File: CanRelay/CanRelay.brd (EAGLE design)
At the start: 70.7 x 62.9 mm, 20 parts

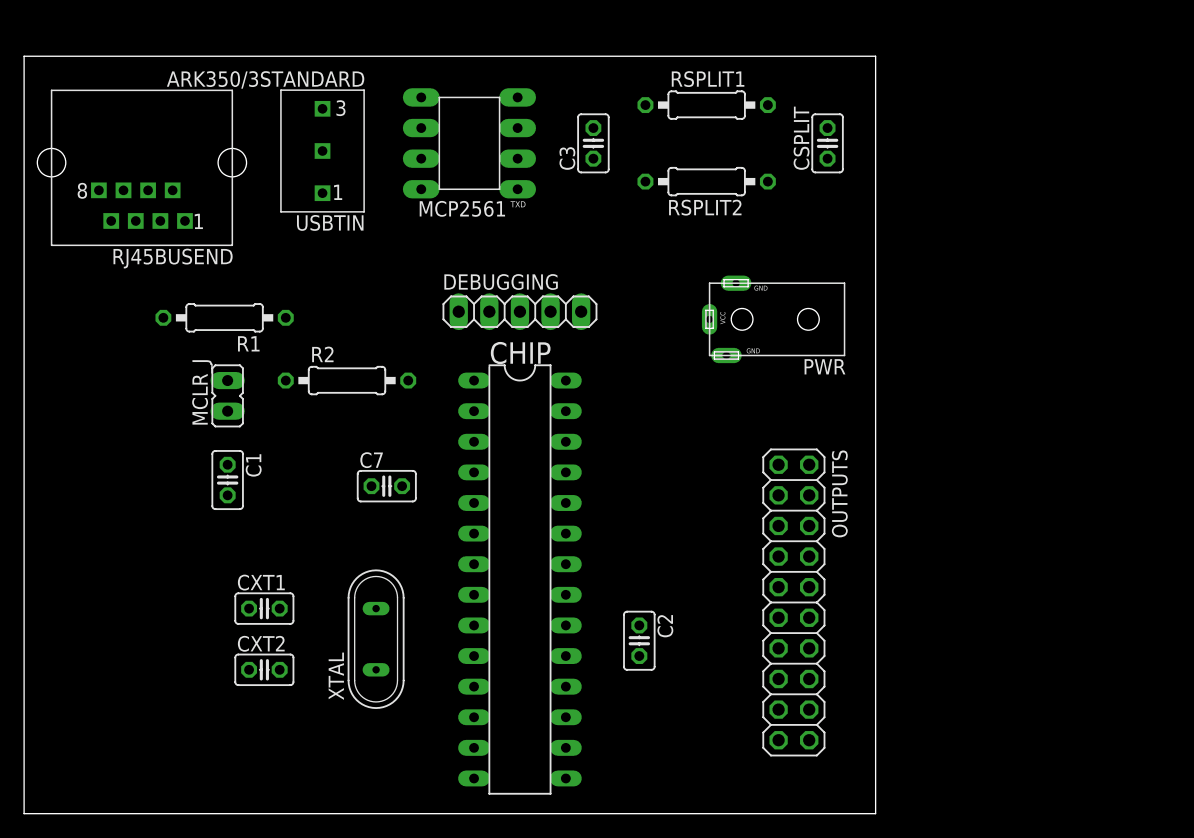
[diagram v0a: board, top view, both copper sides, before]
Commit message: first draft version of the board with routed everything and copper ground too
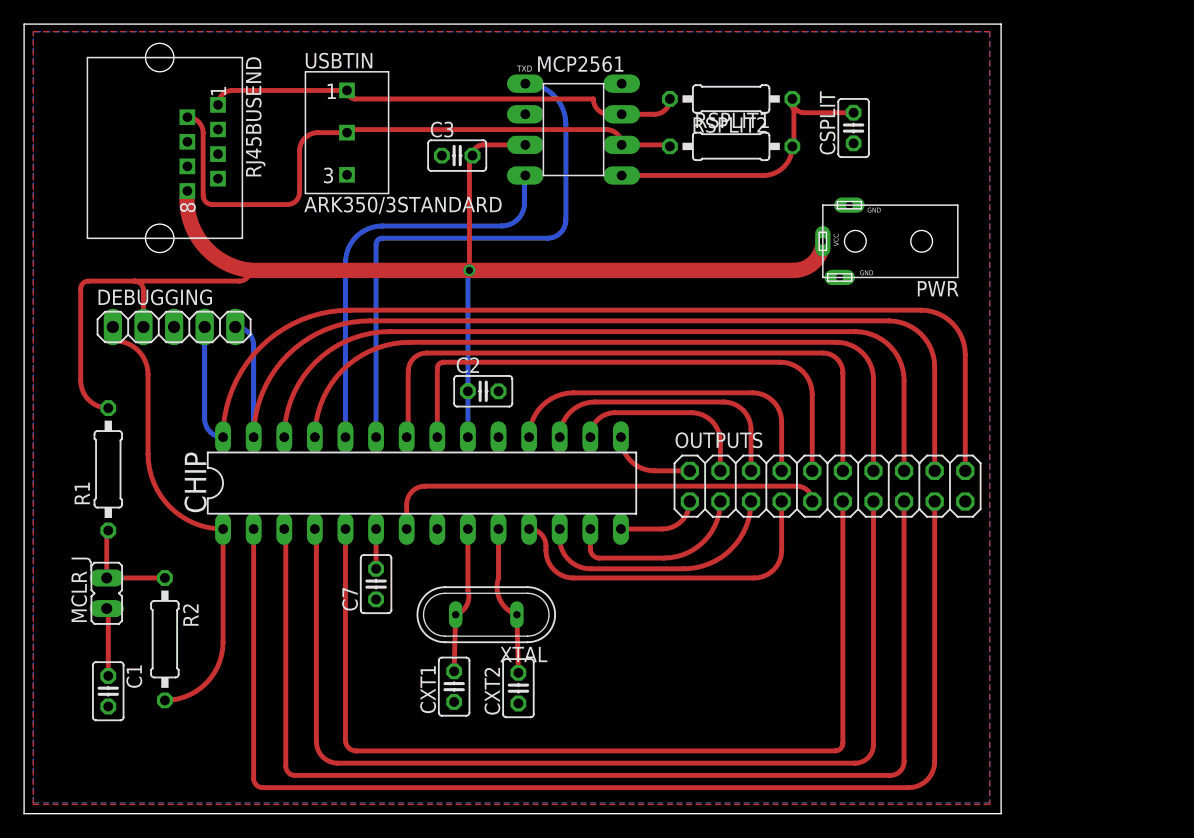
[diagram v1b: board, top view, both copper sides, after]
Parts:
- moved DEBUGGING 28.7 mm to (12.4, 40.4)
- moved R2 26.3 mm to (11.7, 14.5), turned to 270 degrees
- moved C2 24.4 mm to (38.1, 35.1), turned to 0 degrees
- moved CXT2 21.1 mm to (41.0, 10.4), turned to 90 degrees
- moved C1 20.1 mm to (6.99, 10.2)
- moved MCLR_J 19.2 mm to (6.86, 18.3)
- moved CXT1 17.0 mm to (35.7, 10.5), turned to 90 degrees
- moved R1 15.9 mm to (6.99, 28.6), turned to 90 degrees
- moved PWR 11.4 mm to (71.9, 47.5)
- moved CHIP 11.4 mm to (33.0, 27.4), turned to 0 degrees
- moved C3 11.3 mm to (35.9, 54.6), turned to 0 degrees
- moved OUTPUTS 10.0 mm to (66.7, 27.2), turned to 0 degrees
- moved XTAL 9.37 mm to (38.4, 16.5), turned to 180 degrees
- moved MCP2561 8.71 mm to (45.6, 56.8), turned to 0 degrees
- moved C7 8.18 mm to (29.2, 19.1), turned to 90 degrees
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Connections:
- net GND: no longer OUTPUTS.20
- net O1: now also OUTPUTS.17; no longer OUTPUTS.1
- net O10: now also OUTPUTS.12; no longer OUTPUTS.7
- net O13: now also OUTPUTS.14; no longer OUTPUTS.8
- net O14: now also OUTPUTS.16; no longer OUTPUTS.9
- net O17: now also OUTPUTS.7; no longer OUTPUTS.12
- net O18: now also OUTPUTS.5; no longer OUTPUTS.13
- net O19: now also OUTPUTS.3; no longer OUTPUTS.14
- net O2: now also OUTPUTS.15; no longer OUTPUTS.2
- net O20: now also OUTPUTS.1; no longer OUTPUTS.15
- net O21: now also OUTPUTS.2; no longer OUTPUTS.16
- net O22: now also OUTPUTS.4; no longer OUTPUTS.17
- net O23: now also OUTPUTS.6; no longer OUTPUTS.18
- net O24: now also OUTPUTS.8; no longer OUTPUTS.19
- net O3: now also OUTPUTS.13; no longer OUTPUTS.3
- net O4: now also OUTPUTS.11; no longer OUTPUTS.4
- net O6: now also OUTPUTS.9; no longer OUTPUTS.5
- net O9: now also OUTPUTS.10; no longer OUTPUTS.6
- net PGC/O15: now also OUTPUTS.18; no longer OUTPUTS.10
- net PGD/O16: now also OUTPUTS.20; no longer OUTPUTS.11
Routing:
- net +5V: track 0.00 -> 114.9 mm, vias 0 -> 1
- net O1: track 0.00 -> 100.0 mm
- net O2: track 0.00 -> 93.4 mm
- net PGD/O16: track 0.00 -> 86.9 mm
- net O3: track 0.00 -> 85.5 mm
- net PGC/O15: track 0.00 -> 80.5 mm
- net O4: track 0.00 -> 79.5 mm
- net O14: track 0.00 -> 64.2 mm
- net O13: track 0.00 -> 58.5 mm
- net CANL: track 0.00 -> 51.2 mm
- net O10: track 0.00 -> 51.0 mm
- net TXD: track 0.00 -> 45.3 mm
- net O9: track 0.00 -> 44.5 mm
- net CANH: track 0.00 -> 39.3 mm
- net O6: track 0.00 -> 36.8 mm
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- added copper zone on layer 1, net GND
- added copper zone on layer 16, net N$3
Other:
- board size 70.7 x 62.9 mm -> 81.1 x 65.5 mm

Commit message: positioned all components nicely on the board and redid all wires thoroughly this time. Also replaced 3pin for usbtin by regular pinhead since that would be easier to plug into the board
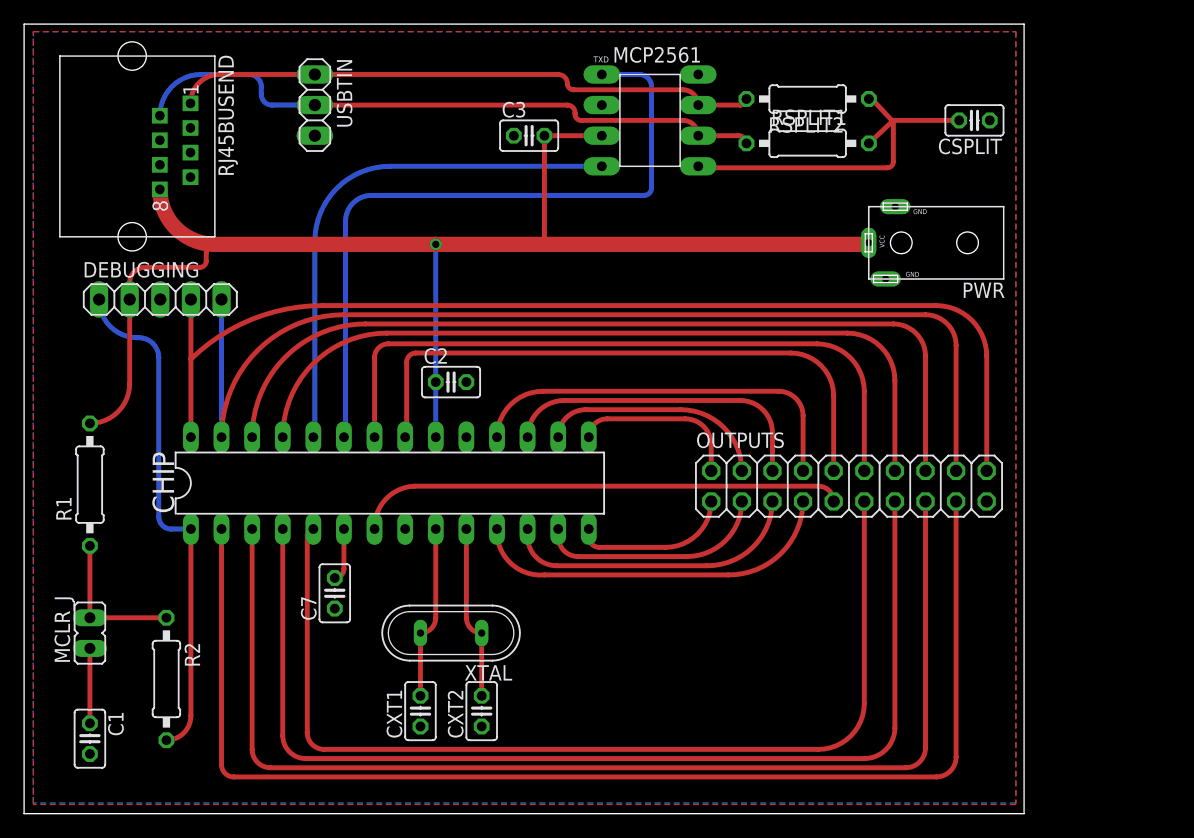
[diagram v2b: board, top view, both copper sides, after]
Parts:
- USBTIN: value ARK350/3STANDARD -> (none); device PoJD:ARK350/3 -> pinhead:1X03
- moved CSPLIT 10.1 mm to (78.9, 57.5), turned to 180 degrees
- moved MCP2561 6.40 mm to (51.9, 57.5)
- moved RSPLIT1 6.36 mm to (65.0, 55.6)
- moved RSPLIT2 6.35 mm to (65.0, 59.3)
- moved C3 6.19 mm to (41.9, 56.3)
- moved C1 4.22 mm to (5.46, 6.22)
- moved PWR 3.81 mm to (75.7, 47.4)
- moved CXT2 3.59 mm to (38.0, 8.51)
- moved MCLR_J 3.59 mm to (5.46, 15.0)
- moved C7 3.51 mm to (25.8, 18.3)
- moved USBTIN 3.51 mm to (24.1, 58.8), turned to 270 degrees
- moved CXT1 3.45 mm to (32.9, 8.51)
- moved R2 3.30 mm to (11.8, 11.2)
- moved XTAL 3.29 mm to (35.4, 15.0)
- moved C2 2.77 mm to (35.4, 35.8)
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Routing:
- net TXD: track 45.3 -> 57.4 mm
- net CANH: track 39.3 -> 48.4 mm
- net RXD: track 33.7 -> 42.7 mm
- net PGC/O15: track 80.5 -> 88.1 mm
- net O21: track 6.87 -> 13.8 mm
- net O14: track 64.2 -> 70.4 mm
- net SPLIT: track 24.8 -> 30.9 mm
- net O20: track 6.66 -> 12.7 mm
- net O9: track 44.5 -> 49.7 mm
- net O13: track 58.5 -> 63.5 mm
- net O10: track 51.0 -> 56.0 mm
- net MCLR: track 36.7 -> 41.6 mm
- net O24: track 27.5 -> 32.4 mm
- net O23: track 21.5 -> 25.9 mm
- net O18: track 20.0 -> 24.1 mm
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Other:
- board size 81.1 x 65.5 mm -> 83 x 65.5 mm

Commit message: added some caption to silkscreen
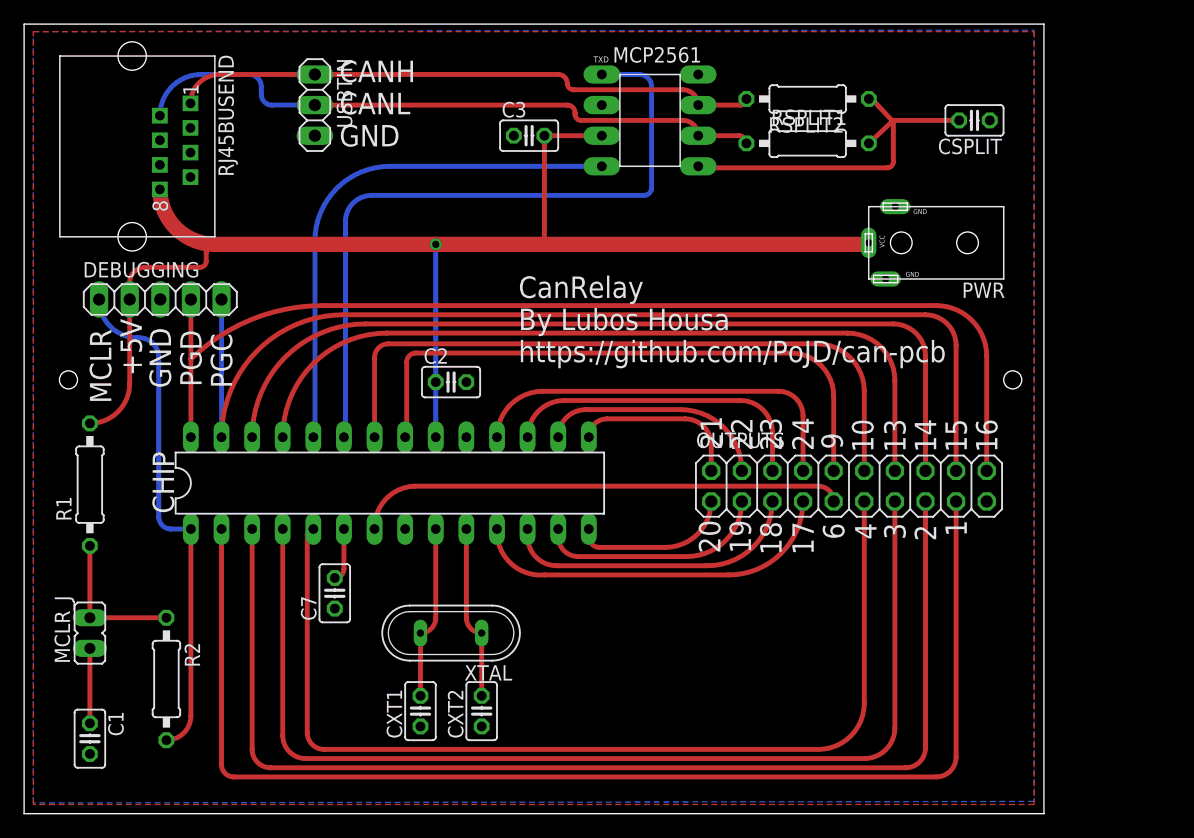
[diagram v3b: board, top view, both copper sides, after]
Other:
- board size 83 x 65.5 mm -> 84.6 x 65.5 mm
- board text added: "+5V"
- board text added: "1"
- board text added: "10"
- board text added: "13"
- board text added: "14"
- board text added: "15"
- board text added: "16"
- board text added: "17"
- board text added: "18"
- board text added: "19"
- board text added: "2"
- board text added: "20"
- board text added: "21"
- board text added: "22"
- board text added: "23"
- board text added: "24"
- board text added: "3"
- board text added: "4"
- board text added: "6"
- board text added: "9"
- board text added: "CANH"
- board text added: "CANL"
- board text added: "CanRelay By Lubos Housa https://github.com/PoJD/can-pcb"
- board text added: "GND"
- board text added: "MCLR"
- board text added: "PGC"
- board text added: "PGD"
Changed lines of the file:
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@@
 <layer number="23" name="tOrigins" color="15" fill="1" visible="yes" active="yes"/>
 <layer number="24" name="bOrigins" color="15" fill="1" visible="yes" active="yes"/>
-<layer number="25" name="tNames" color="7" fill="1" visible="yes" active="yes"/>
-<layer number="26" name="bNames" color="7" fill="1" visible="yes" active="yes"/>
+<layer number="25" name="tNames" color="7" fill="1" visible="no" active="yes"/>
+<layer number="26" name="bNames" color="7" fill="1" visible="no" active="yes"/>
 <layer number="27" name="tValues" color="7" fill="1" visible="yes" active="yes"/>
 <layer number="28" name="bValues" color="7" fill="1" visible="yes" active="yes"/>
@@
 <layer number="43" name="vRestrict" color="2" fill="10" visible="yes" active="yes"/>
 <layer number="44" name="Drills" color="7" fill="1" visible="no" active="yes"/>
-<layer number="45" name="Holes" color="7" fill="1" visible="no" active="yes"/>
+<layer number="45" name="Holes" color="7" fill="1" visible="yes" active="yes"/>
 <layer number="46" name="Milling" color="3" fill="1" visible="no" active="yes"/>
 <layer number="47" name="Measures" color="7" fill="1" visible="no" active="yes"/>
@@
 <board>
 <plain>
-<wire x1="0" y1="0" x2="82.982" y2="0" width="0" layer="20"/>
-<wire x1="82.982" y1="0" x2="82.982" y2="65.522" width="0" layer="20"/>
-<wire x1="82.982" y1="65.522" x2="0" y2="65.522" width="0" layer="20"/>
+<wire x1="0" y1="0" x2="84.633" y2="0" width="0" layer="20"/>
+<wire x1="84.633" y1="0" x2="84.633" y2="65.522" width="0" layer="20"/>
+<wire x1="84.633" y1="65.522" x2="0" y2="65.522" width="0" layer="20"/>
 <wire x1="0" y1="65.522" x2="0" y2="0" width="0" layer="20"/>
+<text x="41.021" y="37.465" size="1.778" layer="21">CanRelay
+By Lubos Housa
+https://github.com/PoJD/can-pcb</text>
+<hole x="3.683" y="36" drill="1.5"/>
+<hole x="82.042" y="36" drill="1.5"/>
+<text x="26.162" y="60.706" size="1.778" layer="21">CANH</text>
+<text x="26.162" y="58.039" size="1.778" layer="21">CANL</text>
+<text x="26.162" y="55.372" size="1.778" layer="21">GND</text>
+<text x="7.239" y="34.036" size="1.778" layer="21" rot="R90">MCLR</text>
+<text x="9.779" y="36.322" size="1.778" layer="21" rot="R90">+5V</text>
+<text x="12.192" y="35.306" size="1.778" layer="21" rot="R90">GND</text>
+<text x="17.272" y="35.306" size="1.778" layer="21" rot="R90">PGC</text>
+<text x="14.732" y="35.433" size="1.778" layer="21" rot="R90">PGD</text>
+<text x="57.912" y="30.226" size="1.778" layer="21" rot="R90">21</text>
+<text x="60.452" y="30.099" size="1.778" layer="21" rot="R90">22</text>
+<text x="62.865" y="30.099" size="1.778" layer="21" rot="R90">23</text>
+<text x="65.532" y="30.099" size="1.778" layer="21" rot="R90">24</text>
+<text x="67.945" y="30.226" size="1.778" layer="21" rot="R90">9</text>
+<text x="70.485" y="29.972" size="1.778" layer="21" rot="R90">10</text>
+<text x="73.152" y="29.972" size="1.778" layer="21" rot="R90">13</text>
+<text x="75.692" y="29.972" size="1.778" layer="21" rot="R90">14</text>
+<text x="78.232" y="29.972" size="1.778" layer="21" rot="R90">15</text>
+<text x="80.772" y="29.972" size="1.778" layer="21" rot="R90">16</text>
+<text x="57.785" y="21.59" size="1.778" layer="21" rot="R90">20</text>
+<text x="60.325" y="21.59" size="1.778" layer="21" rot="R90">19</text>
+<text x="62.865" y="21.463" size="1.778" layer="21" rot="R90">18</text>
+<text x="65.532" y="21.463" size="1.778" layer="21" rot="R90">17</text>
+<text x="68.072" y="22.733" size="1.778" layer="21" rot="R90">6</text>
+<text x="70.739" y="22.733" size="1.778" layer="21" rot="R90">4</text>
+<text x="73.152" y="22.733" size="1.778" layer="21" rot="R90">3</text>
+<text x="75.692" y="22.606" size="1.778" layer="21" rot="R90">2</text>
+<text x="78.232" y="22.987" size="1.778" layer="21" rot="R90">1</text>
 </plain>
 <attributes>
@@
 <polygon width="0.254" layer="1">
 <vertex x="0.762" y="64.897"/>
-<vertex x="82.296" y="64.897"/>
-<vertex x="82.296" y="0.762"/>
+<vertex x="83.82" y="64.897"/>
+<vertex x="83.82" y="0.762"/>
 <vertex x="0.762" y="0.762"/>
 </polygon>
@@
 <polygon width="0.254" layer="16">
 <vertex x="0.762" y="64.897"/>
-<vertex x="82.296" y="64.897"/>
-<vertex x="82.296" y="0.889"/>
+<vertex x="83.82" y="65.024"/>
+<vertex x="83.82" y="1.016"/>
 <vertex x="0.762" y="0.889"/>
 </polygon>
@@
 </board>
 </drawing>
+<compatibility>
+<note version="6.3" minversion="6.2.2" severity="warning">
+Since Version 6.2.2 text objects can contain more than one line,
+which will not be processed correctly with this version.
+</note>
+</compatibility>
 </eagle>
